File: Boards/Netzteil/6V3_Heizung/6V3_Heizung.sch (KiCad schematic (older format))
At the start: 36 parts, among them P1 7V5_AC, P2 12V_DC, P3 6V3_DC_1, P4 6V3_DC_2, Q1 IRF540N, Q2 IRF540N, U1 TL072

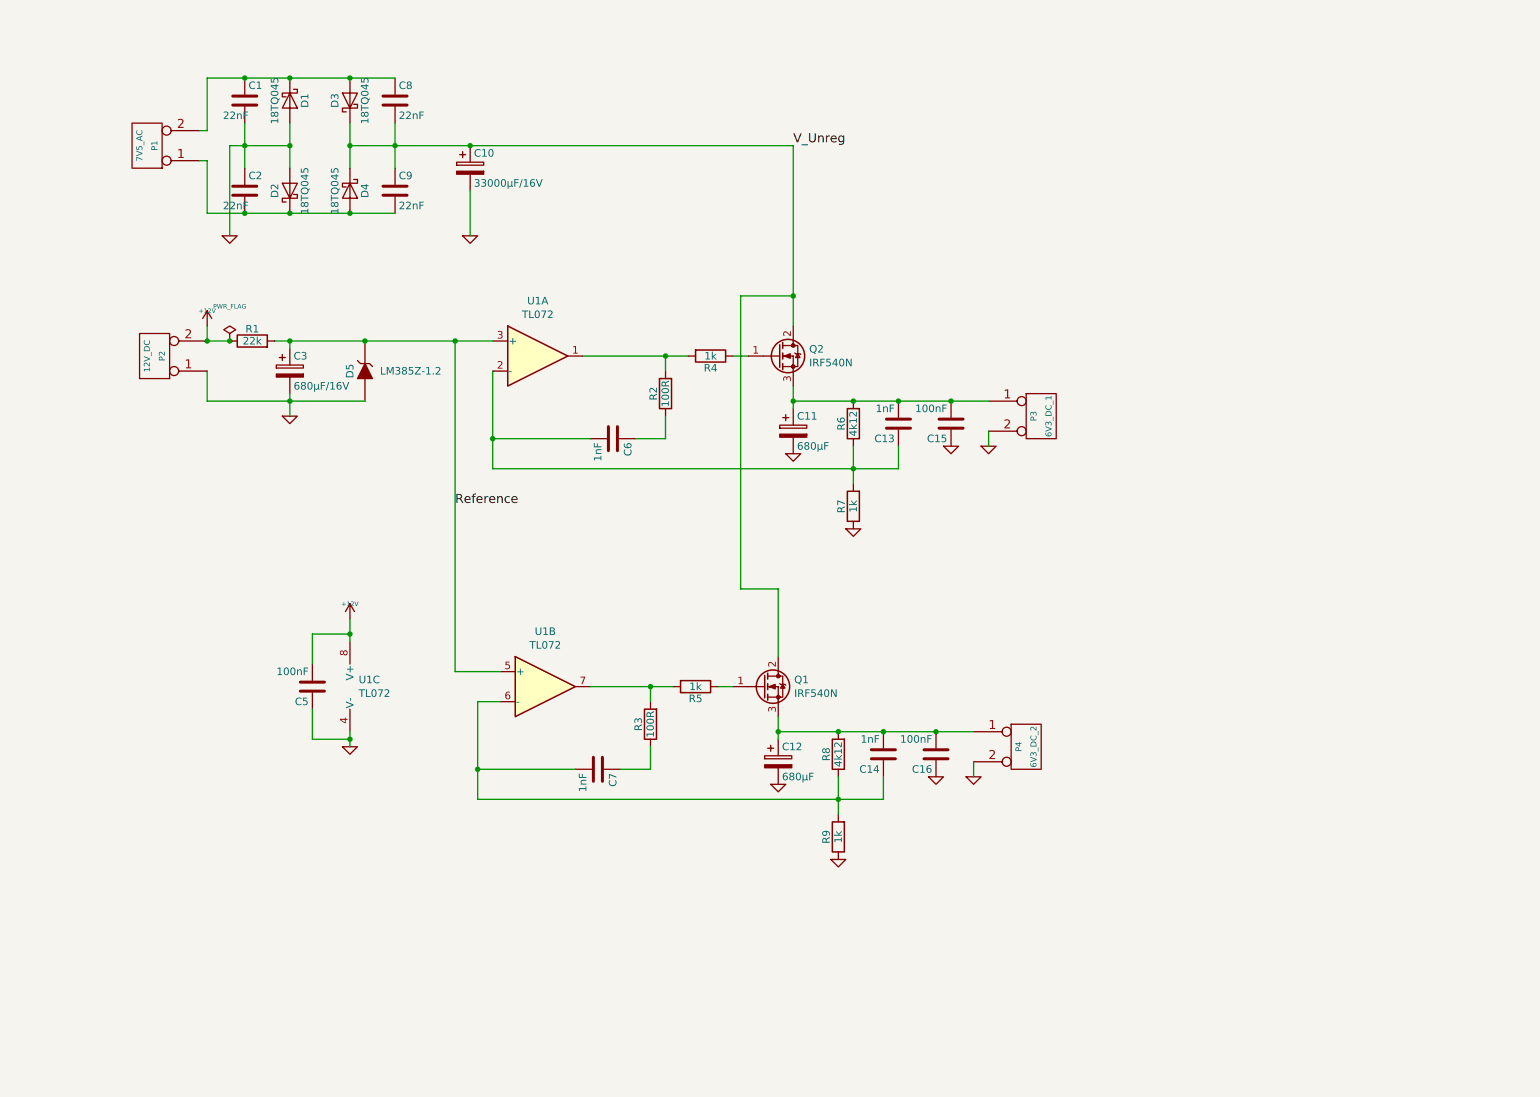
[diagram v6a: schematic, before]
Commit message: HV Switch on delay added
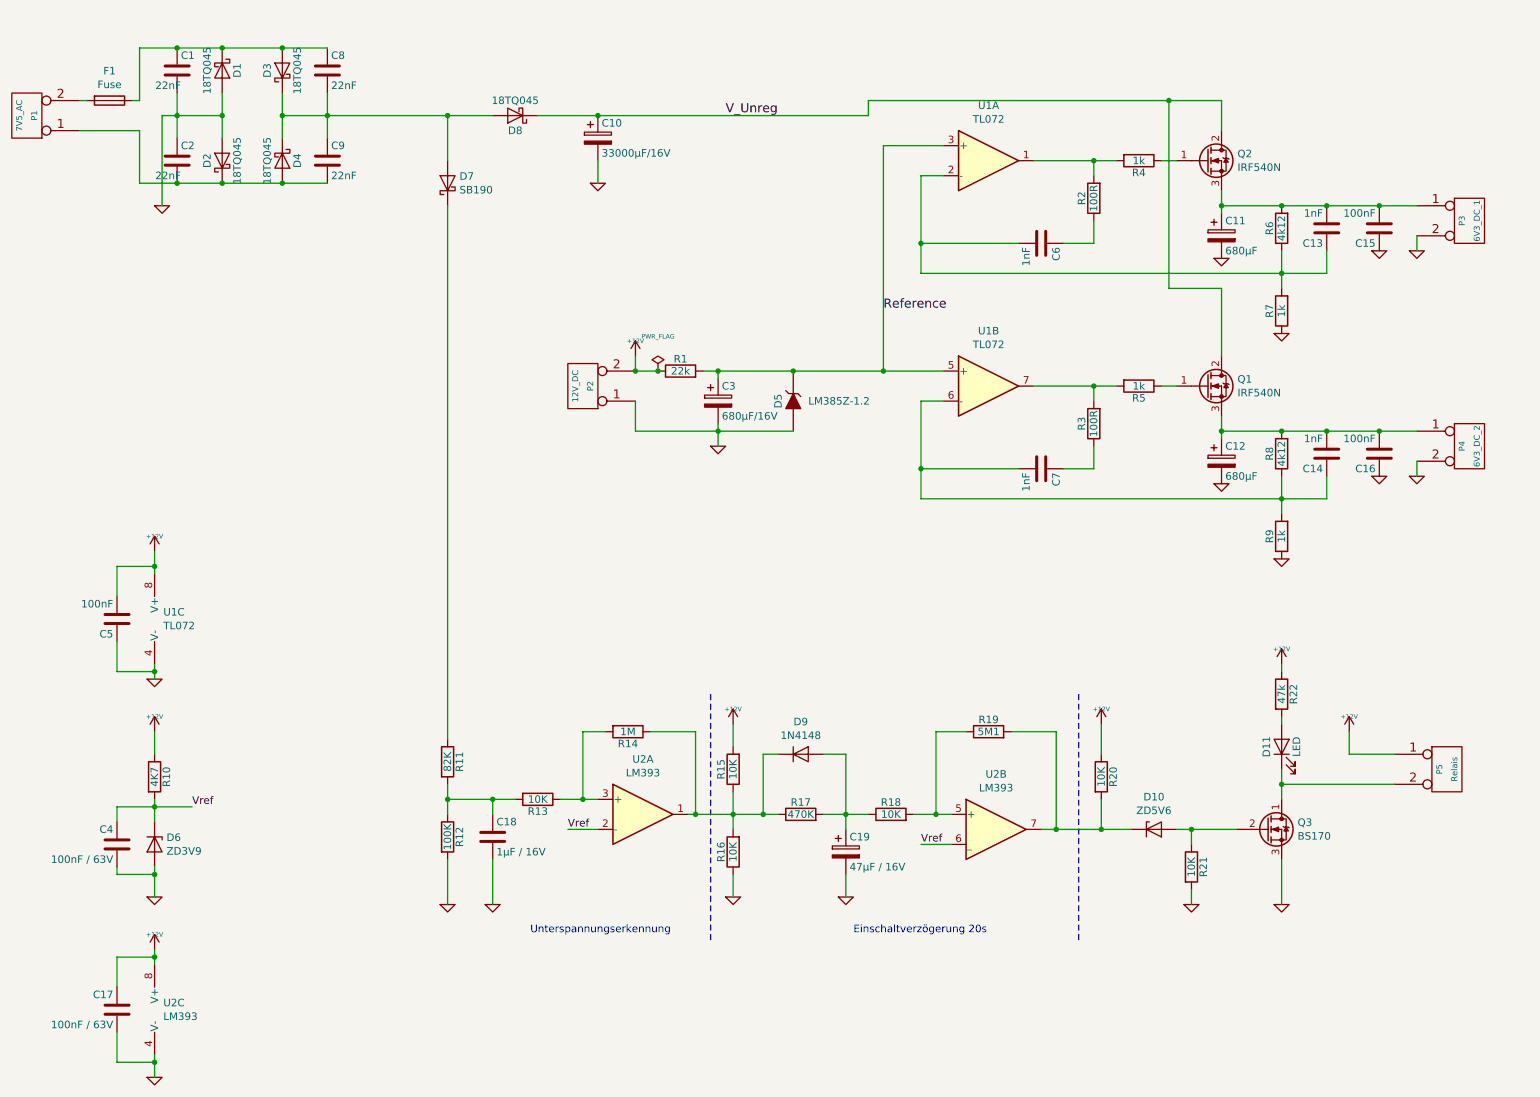
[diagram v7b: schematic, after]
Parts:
- added C17, C4: 100nF / 63V, Capacitor_THT:C_Disc_D3.0mm_W2.0mm_P2.50mm, symbol Device:C
- added C18: 1µF / 16V, Capacitor_THT:C_Disc_D3.0mm_W2.0mm_P2.50mm, symbol Device:C
- added C19: 47µF / 16V, Capacitor_THT:CP_Radial_D8.0mm_P3.80mm, symbol Device:CP
- added D10: ZD5V6, Diode_THT:D_DO-35_SOD27_P10.16mm_Horizontal, symbol Device:D_Zener
- added D11: LED, LED_THT:LED_D3.0mm, symbol Device:LED
- added D6: ZD3V9, Diode_THT:D_DO-35_SOD27_P10.16mm_Horizontal, symbol Device:D_Zener
- added D7: SB190, Diode_THT:D_DO-41_SOD81_P10.16mm_Horizontal, symbol Diode:SB160
- added D8: 18TQ045, Package_TO_SOT_THT:TO-220-2_Vertical, symbol Device:D_Schottky
- added D9: 1N4148, Diode_THT:D_DO-35_SOD27_P10.16mm_Horizontal, symbol Diode:1N4148
- added F1: Fuse, w_misc_comp:fuse_holder_CQ-2, symbol Device:Fuse
- added P5: Relais, Connector_Molex:Molex_KK-254_AE-6410-02A_1x02_P2.54mm_Vertical, symbol 6V3_Heizung-rescue:CONN_2-12V_Supply_V2-rescue
- added Q3: BS170, Package_TO_SOT_THT:TO-92_Inline, symbol Transistor_FET:BS170
- added R10: 4K7, Resistor_THT:R_Axial_DIN0207_L6.3mm_D2.5mm_P10.16mm_Horizontal, symbol Device:R
- added R11: 82K, Resistor_THT:R_Axial_DIN0207_L6.3mm_D2.5mm_P10.16mm_Horizontal, symbol Device:R
- added R12: 100K, Resistor_THT:R_Axial_DIN0207_L6.3mm_D2.5mm_P10.16mm_Horizontal, symbol Device:R
- added R13, R15, R16, R18, R20, R21: 10K, Resistor_THT:R_Axial_DIN0207_L6.3mm_D2.5mm_P10.16mm_Horizontal, symbol Device:R
- added R14: 1M, Resistor_THT:R_Axial_DIN0207_L6.3mm_D2.5mm_P10.16mm_Horizontal, symbol Device:R
- added R17: 470K, Resistor_THT:R_Axial_DIN0207_L6.3mm_D2.5mm_P10.16mm_Horizontal, symbol Device:R
- added R19: 5M1, Resistor_THT:R_Axial_DIN0207_L6.3mm_D2.5mm_P10.16mm_Horizontal, symbol Device:R
- added R22: 47k, Resistor_THT:R_Axial_DIN0207_L6.3mm_D2.5mm_P10.16mm_Horizontal, symbol Device:R
- added U2: LM393, Package_DIP:DIP-8_W7.62mm, symbol Comparator:LM393
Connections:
- net +12V: now also C17.1, P5.1 (P1), R10.1, R15.2, R20.1, R22.1, U2.8 (V+)
- net GND: now also C17.2, C18.2, C19.2, C4.2, D6.2 (A), Q3.3 (S), R12.2, R16.1, R21.2, U2.4 (V-)
- net V_Unreg: now also D8.1 (K); no longer C8.2, C9.1, D3.1 (K), D4.1 (K)
- net at C1.1, C8.1, D1.1 (K)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: now also F1.1; no longer P1.2 (P2)
- new net: F1.2, P1.2 (P2)
- new net: C8.2, C9.1, D3.1 (K), D4.1 (K), D7.2 (A), D8.2 (A)
- new net: D11.1 (K), P5.2 (P2), Q3.1 (D)
- new net: D11.2 (A), R22.2
- new net: D9.1 (K), R14.1, R15.1, R16.2, R17.1, U2.1
- new net: R13.1, R14.2, U2.3 (+)
- new net: R18.2, R19.1, U2.5 (+)
- new net: D10.1 (K), R19.2, R20.2, U2.7
- new net: D7.1 (K), R11.1
- new net: C18.1, R11.2, R12.1, R13.2
- new net: C19.1, D9.2 (A), R17.2, R18.1
- new net: D10.2 (A), Q3.2 (G), R21.1
- new net Vref: C4.1, D6.1 (K), R10.2, U2.2 (-), U2.6 (_)
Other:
- note added: "Einschaltverzögerung 20s"
- note added: "Unterspannungserkennung"
- moved on the sheet: C1, C10, C11, C12, C13, C14, C15, C16, C2, C3, C5, C6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

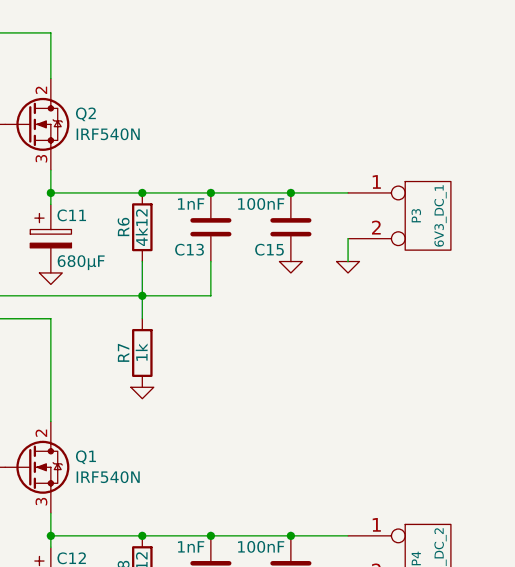
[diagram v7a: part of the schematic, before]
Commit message: Added Power LEDs
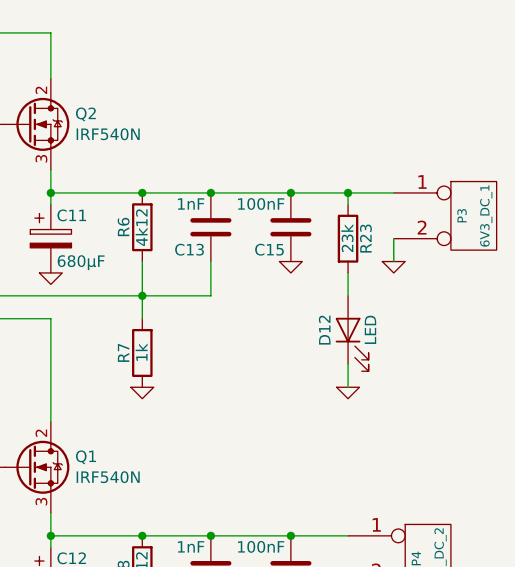
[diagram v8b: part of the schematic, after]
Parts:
- added D12: LED, LED_THT:LED_D3.0mm, symbol Device:LED
- added R23: 23k, Resistor_THT:R_Axial_DIN0207_L6.3mm_D2.5mm_P10.16mm_Horizontal, symbol Device:R
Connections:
- net GND: now also D12.1 (K)
- net at C11.1, C13.2, C15.2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: now also R23.1
- new net: D12.2 (A), R23.2
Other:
- moved on the sheet: P3
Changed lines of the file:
@@
 L 6V3_Heizung-rescue:CONN_2-borniers P3
 U 1 1 55C67667
-P 10200 1850
-F 0 "P3" V 10150 1850 40  0000 C CNN
-F 1 "6V3_DC_1" V 10250 1850 40  0000 C CNN
-F 2 "Connector_TE-Connectivity:TE_MATE-N-LOK_1-770866-x_1x02_P4.14mm_Vertical" H 10200 1850 60  0001 C CNN
-F 3 "" H 10200 1850 60  0000 C CNN
-	1    10200 1850
+P 10400 1850
+F 0 "P3" V 10350 1850 40  0000 C CNN
+F 1 "6V3_DC_1" V 10450 1850 40  0000 C CNN
+F 2 "Connector_TE-Connectivity:TE_MATE-N-LOK_1-770866-x_1x02_P4.14mm_Vertical" H 10400 1850 60  0001 C CNN
+F 3 "" H 10400 1850 60  0000 C CNN
+	1    10400 1850
 	1    0    0    -1
 $EndComp
@@
 L 6V3_Heizung-rescue:GND-RESCUE-6V3_Heizung #PWR015
 U 1 1 55C6766E
-P 9850 2050
-F 0 "#PWR015" H 9850 2050 30  0001 C CNN
-F 1 "GND" H 9850 1980 30  0001 C CNN
-F 2 "" H 9850 2050 60  0000 C CNN
-F 3 "" H 9850 2050 60  0000 C CNN
-	1    9850 2050
-	1    0    0    -1
-$EndComp
-Wire Wire Line
-	9850 1950 9850 2050
+P 10050 2050
+F 0 "#PWR015" H 10050 2050 30  0001 C CNN
+F 1 "GND" H 10050 1980 30  0001 C CNN
+F 2 "" H 10050 2050 60  0000 C CNN
+F 3 "" H 10050 2050 60  0000 C CNN
+	1    10050 2050
+	1    0    0    -1
+$EndComp
+Wire Wire Line
+	10050 1950 10050 2050
 $Comp
 L power:PWR_FLAG #FLG016
@@
 Wire Wire Line
 	1000 1050 950  1050
+$Comp
+L Device:LED D12
+U 1 1 5DFDA5E8
+P 9850 2350
+F 0 "D12" H 9850 2450 50  0000 C CNN
+F 1 "LED" H 9850 2250 50  0000 C CNN
+F 2 "LED_THT:LED_D3.0mm" H 9850 2350 50  0001 C CNN
+F 3 "" H 9850 2350 50  0001 C CNN
+	1    9850 2350
+	0    -1   -1   0
+$EndComp
+$Comp
+L Device:R R23
+U 1 1 5DFDB2EF
+P 9850 1950
+F 0 "R23" V 9930 1950 50  0000 C CNN
+F 1 "23k" V 9850 1950 50  0000 C CNN
+F 2 "Resistor_THT:R_Axial_DIN0207_L6.3mm_D2.5mm_P10.16mm_Horizontal" V 9780 1950 30  0001 C CNN
+F 3 "" H 9850 1950 30  0000 C CNN
+	1    9850 1950
+	1    0    0    -1
+$EndComp
+$Comp
+L 6V3_Heizung-rescue:GND-RESCUE-6V3_Heizung #PWR0116
+U 1 1 5DFFF90A
+P 9850 2600
+F 0 "#PWR0116" H 9850 2600 30  0001 C CNN
+F 1 "GND" H 9850 2530 30  0001 C CNN
+F 2 "" H 9850 2600 60  0000 C CNN
+F 3 "" H 9850 2600 60  0000 C CNN
+	1    9850 2600
+	1    0    0    -1
+$EndComp
+Wire Wire Line
+	9850 2200 9850 2100
+Wire Wire Line
+	9850 1800 9850 1750
+Connection ~ 9850 1750
+Wire Wire Line
+	9850 1750 10050 1750
+Wire Wire Line
+	9850 2600 9850 2500
 $EndSCHEMATC
